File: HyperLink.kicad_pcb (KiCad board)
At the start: 2 copper layers, 35 x 24 mm, 45 parts, among them J1 USB_C_Receptacle_USB2.0, J2 Conn_02x05_Odd_Even, J3 Conn_02x05_Odd_Even, SW1 SW_Push, U1 ESP32-C3, U2 PESD2USB5UXT, U3 MIC5504-3.3YM5, Y1 ABM11W-40.0000MHZ-8-B1U-T3

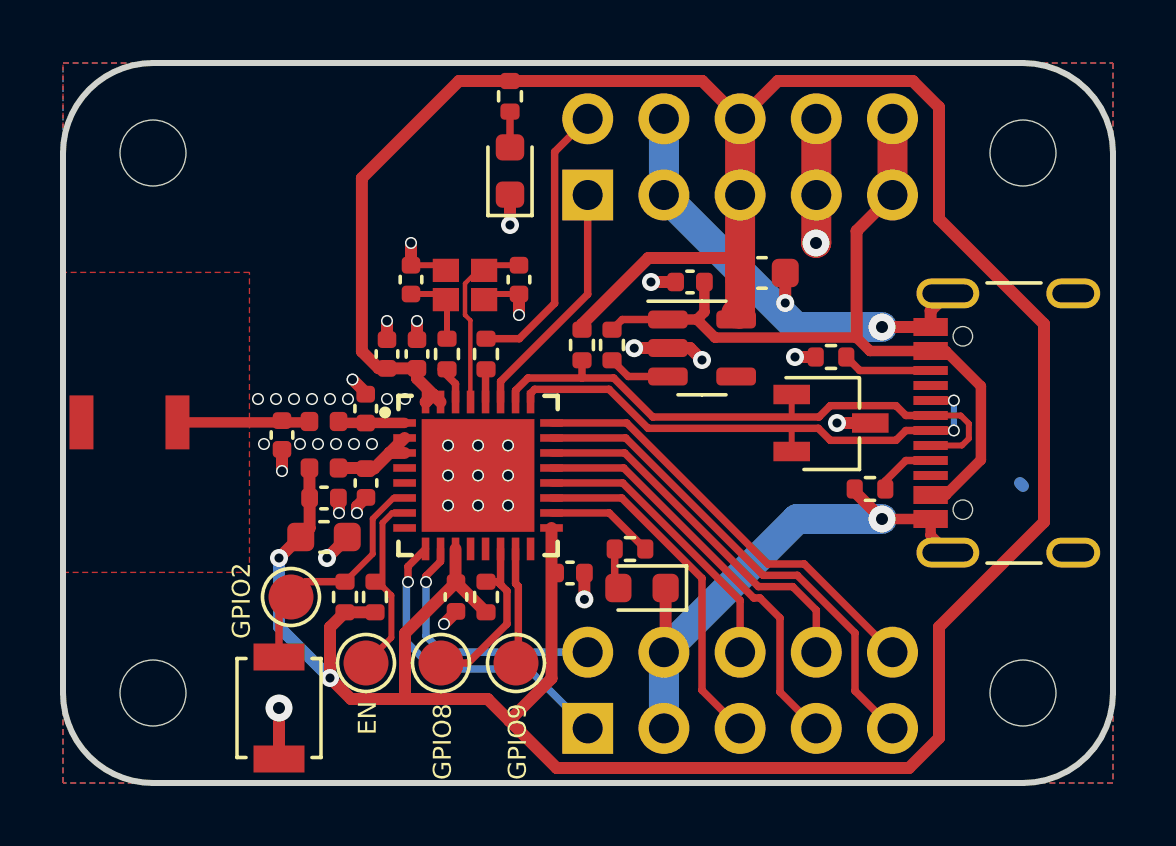
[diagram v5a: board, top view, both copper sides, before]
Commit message: Add via stitching
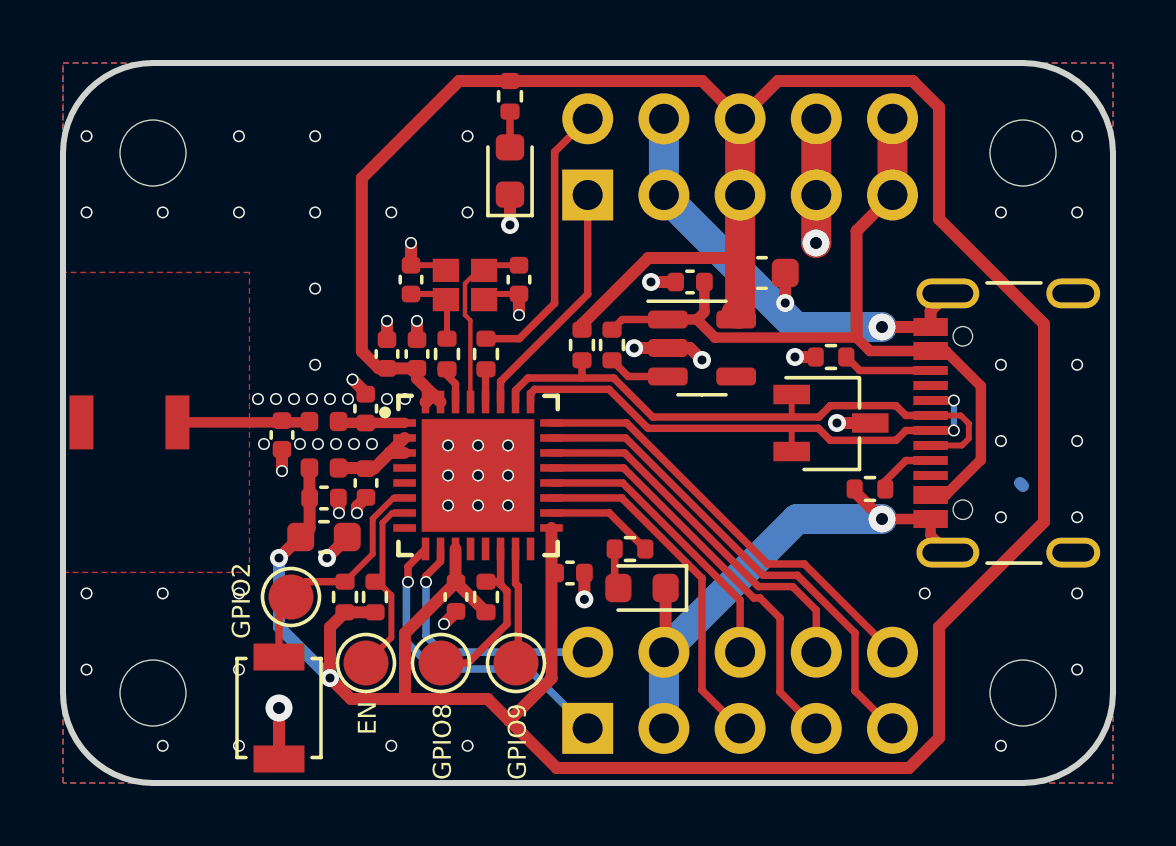
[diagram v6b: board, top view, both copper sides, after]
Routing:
- net GND: vias 45 -> 79
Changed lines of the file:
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@@
   (segment (start 132.1 88.3) (end 132.1 88.28) (width 0.4) (layer "F.Cu") (net 5))
   (segment (start 144.11 75.99) (end 144.1 76) (width 1) (layer "F.Cu") (net 5))
+  (via (at 127.405 74.979999) (size 0.4) (drill 0.3) (layers "F.Cu" "B.Cu") (free) (net 5))
+  (via (at 132.485 72.439999) (size 0.4) (drill 0.3) (layers "F.Cu" "B.Cu") (free) (net 5))
+  (via (at 122.325 92.759999) (size 0.4) (drill 0.3) (layers "F.Cu" "B.Cu") (free) (net 5))
   (via (at 130.4 81.2) (size 0.4) (drill 0.3) (layers "F.Cu" "B.Cu") (free) (net 5))
   (via (at 128.65 80.55) (size 0.4) (drill 0.3) (layers "F.Cu" "B.Cu") (free) (net 5))
   (via (at 126.9 82.7) (size 0.4) (drill 0.3) (layers "F.Cu" "B.Cu") (free) (net 5))
+  (via (at 119.785 72.439999) (size 0.4) (drill 0.3) (layers "F.Cu" "B.Cu") (free) (net 5))
   (via (at 138.6 77.3) (size 0.6) (drill 0.3) (layers "F.Cu" "B.Cu") (net 5))
   (via (at 129.8 81.2) (size 0.4) (drill 0.3) (layers "F.Cu" "B.Cu") (free) (net 5))
+  (via (at 152.805 87.679999) (size 0.4) (drill 0.3) (layers "F.Cu" "B.Cu") (free) (net 5))
+  (via (at 147.725 87.679999) (size 0.4) (drill 0.3) (layers "F.Cu" "B.Cu") (free) (net 5))
   (via (at 133.9 75.4) (size 0.6) (drill 0.3) (layers "F.Cu" "B.Cu") (net 5))
   (via (at 128.1 82.7) (size 0.4) (drill 0.3) (layers "F.Cu" "B.Cu") (free) (net 5))
+  (via (at 124.865 92.759999) (size 0.4) (drill 0.3) (layers "F.Cu" "B.Cu") (free) (net 5))
+  (via (at 132.485 74.979999) (size 0.4) (drill 0.3) (layers "F.Cu" "B.Cu") (free) (net 5))
   (via (at 146.3 78.8) (size 0.9) (drill 0.4) (layers "F.Cu" "B.Cu") (free) (net 5))
   (via (at 133.834851 84.7487) (size 0.4) (drill 0.3) (layers "F.Cu" "B.Cu") (net 5))
@@
   (via (at 131.834851 84.7487) (size 0.4) (drill 0.3) (layers "F.Cu" "B.Cu") (net 5))
   (via (at 127.5 82.7) (size 0.4) (drill 0.3) (layers "F.Cu" "B.Cu") (free) (net 5))
+  (via (at 152.805 74.979999) (size 0.4) (drill 0.3) (layers "F.Cu" "B.Cu") (free) (net 5))
+  (via (at 127.405 80.059999) (size 0.4) (drill 0.3) (layers "F.Cu" "B.Cu") (free) (net 5))
   (via (at 136.38 87.88) (size 0.6) (drill 0.3) (layers "F.Cu" "B.Cu") (free) (net 5))
   (via (at 143.075 78) (size 0.6) (drill 0.3) (layers "F.Cu" "B.Cu") (net 5))
   (via (at 138.040639 79.505918) (size 0.6) (drill 0.3) (layers "F.Cu" "B.Cu") (net 5))
   (via (at 131.834851 83.7487) (size 0.4) (drill 0.3) (layers "F.Cu" "B.Cu") (net 5))
+  (via (at 124.865 72.439999) (size 0.4) (drill 0.3) (layers "F.Cu" "B.Cu") (free) (net 5))
   (via (at 144.8 82) (size 0.6) (drill 0.3) (layers "F.Cu" "B.Cu") (net 5))
   (via (at 132.834851 82.7487) (size 0.4) (drill 0.3) (layers "F.Cu" "B.Cu") (net 5))
+  (via (at 124.865 74.979999) (size 0.4) (drill 0.3) (layers "F.Cu" "B.Cu") (free) (net 5))
   (via (at 130.6 76) (size 0.4) (drill 0.3) (layers "F.Cu" "B.Cu") (free) (net 5))
+  (via (at 150.265 74.979999) (size 0.4) (drill 0.3) (layers "F.Cu" "B.Cu") (free) (net 5))
+  (via (at 124.865 87.679999) (size 0.4) (drill 0.3) (layers "F.Cu" "B.Cu") (free) (net 5))
   (via (at 126.2 91.5) (size 0.9) (drill 0.4) (layers "F.Cu" "B.Cu") (net 5))
+  (via (at 150.265 92.759999) (size 0.4) (drill 0.3) (layers "F.Cu" "B.Cu") (free) (net 5))
   (via (at 128.799503 85) (size 0.4) (drill 0.3) (layers "F.Cu" "B.Cu") (free) (net 5))
+  (via (at 127.405 72.439999) (size 0.4) (drill 0.3) (layers "F.Cu" "B.Cu") (free) (net 5))
   (via (at 143.4 79.8) (size 0.6) (drill 0.3) (layers "F.Cu" "B.Cu") (net 5))
+  (via (at 119.785 87.679999) (size 0.4) (drill 0.3) (layers "F.Cu" "B.Cu") (free) (net 5))
   (via (at 133.834851 83.7487) (size 0.4) (drill 0.3) (layers "F.Cu" "B.Cu") (net 5))
+  (via (at 152.805 90.219999) (size 0.4) (drill 0.3) (layers "F.Cu" "B.Cu") (free) (net 5))
+  (via (at 152.805 85.139999) (size 0.4) (drill 0.3) (layers "F.Cu" "B.Cu") (free) (net 5))
   (via (at 131.834851 82.7487) (size 0.4) (drill 0.3) (layers "F.Cu" "B.Cu") (net 5))
   (via (at 127.3 81.2) (size 0.4) (drill 0.3) (layers "F.Cu" "B.Cu") (free) (net 5))
+  (via (at 122.325 87.679999) (size 0.4) (drill 0.3) (layers "F.Cu" "B.Cu") (free) (net 5))
+  (via (at 119.785 90.219999) (size 0.4) (drill 0.3) (layers "F.Cu" "B.Cu") (free) (net 5))
   (via (at 128.7 82.7) (size 0.4) (drill 0.3) (layers "F.Cu" "B.Cu") (free) (net 5))
+  (via (at 152.805 80.059999) (size 0.4) (drill 0.3) (layers "F.Cu" "B.Cu") (free) (net 5))
   (via (at 129.8 78.6) (size 0.4) (drill 0.3) (layers "F.Cu" "B.Cu") (free) (net 5))
   (via (at 132.834851 84.7487) (size 0.4) (drill 0.3) (layers "F.Cu" "B.Cu") (net 5))
+  (via (at 122.325 74.979999) (size 0.4) (drill 0.3) (layers "F.Cu" "B.Cu") (free) (net 5))
   (via (at 126.3 83.6) (size 0.4) (drill 0.3) (layers "F.Cu" "B.Cu") (free) (net 5))
+  (via (at 152.805 82.599999) (size 0.4) (drill 0.3) (layers "F.Cu" "B.Cu") (free) (net 5))
+  (via (at 129.945 92.759999) (size 0.4) (drill 0.3) (layers "F.Cu" "B.Cu") (free) (net 5))
   (via (at 130.8 78.6) (size 0.4) (drill 0.3) (layers "F.Cu" "B.Cu") (free) (net 5))
   (via (at 146.3 85.2) (size 0.9) (drill 0.4) (layers "F.Cu" "B.Cu") (free) (net 5))
   (via (at 125.7 82.7) (size 0.4) (drill 0.3) (layers "F.Cu" "B.Cu") (free) (net 5))
+  (via (at 150.265 85.139999) (size 0.4) (drill 0.3) (layers "F.Cu" "B.Cu") (free) (net 5))
   (via (at 140.3 79.9) (size 0.6) (drill 0.3) (layers "F.Cu" "B.Cu") (net 5))
+  (via (at 132.485 92.759999) (size 0.4) (drill 0.3) (layers "F.Cu" "B.Cu") (free) (net 5))
   (via (at 128.2 85) (size 0.4) (drill 0.3) (layers "F.Cu" "B.Cu") (free) (net 5))
+  (via (at 129.945 74.979999) (size 0.4) (drill 0.3) (layers "F.Cu" "B.Cu") (free) (net 5))
   (via (at 129.3 82.7) (size 0.4) (drill 0.3) (layers "F.Cu" "B.Cu") (free) (net 5))
+  (via (at 119.785 74.979999) (size 0.4) (drill 0.3) (layers "F.Cu" "B.Cu") (free) (net 5))
   (via (at 126.099503 81.2) (size 0.4) (drill 0.3) (layers "F.Cu" "B.Cu") (free) (net 5))
   (via (at 144.1 76) (size 0.9) (drill 0.4) (layers "F.Cu" "B.Cu") (free) (net 5))
@@
   (via (at 125.5 81.2) (size 0.4) (drill 0.3) (layers "F.Cu" "B.Cu") (free) (net 5))
   (via (at 131.7 88.7) (size 0.4) (drill 0.3) (layers "F.Cu" "B.Cu") (free) (net 5))
+  (via (at 152.805 72.439999) (size 0.4) (drill 0.3) (layers "F.Cu" "B.Cu") (free) (net 5))
   (via (at 127.9 81.2) (size 0.4) (drill 0.3) (layers "F.Cu" "B.Cu") (free) (net 5))
+  (via (at 124.865 90.219999) (size 0.4) (drill 0.3) (layers "F.Cu" "B.Cu") (free) (net 5))
   (via (at 128.5 81.2) (size 0.4) (drill 0.3) (layers "F.Cu" "B.Cu") (free) (net 5))
   (via (at 127.8 86.5) (size 0.6) (drill 0.3) (layers "F.Cu" "B.Cu") (free) (net 5))
+  (via (at 150.265 80.059999) (size 0.4) (drill 0.3) (layers "F.Cu" "B.Cu") (free) (net 5))
+  (via (at 150.265 82.599999) (size 0.4) (drill 0.3) (layers "F.Cu" "B.Cu") (free) (net 5))
+  (via (at 127.405 77.519999) (size 0.4) (drill 0.3) (layers "F.Cu" "B.Cu") (free) (net 5))
   (segment (start 143.43 78.8) (end 146.3 78.8) (width 1) (layer "B.Cu") (net 5))
   (segment (start 139.03 92.18) (end 139.03 89.64) (width 1) (layer "B.Cu") (net 5))
@@
     )
   )
+  (group "ViaStitching GND" (id 121eea07-2583-43eb-af17-1480b4d71986)
+    (members
+      00bb237d-837b-4d5a-bcef-fa8cfbdb1b4f
+      06f155e1-c9e6-4bee-978f-681a4968c2e1
+      08c9f7d6-f1ce-4e30-9afb-da5f94dd47ce
+      0e67f340-c2e4-46b6-9b0b-a6d67aab93a5
+      220ef5ba-ac45-4e73-99d3-577b26c0473a
+      23bdd84b-9662-4baf-8c54-9a2bf71ae2ce
+      2ef98852-6df9-4ee1-8d35-f6a4a30a555b
+      31b7294f-a97f-4f42-8ae6-3d87eb07fe97
+      4b072cb5-440d-463b-9ff8-211d0f28688c
+      4ddd4fa3-a042-4c53-b063-b147359e3cbb
+      557f1756-ca36-4d67-9c0f-42117ab397c9
+      64ec0c78-07fc-4cba-ac41-35cad36918ec
+      66550240-bda5-475f-a09d-6517f8722017
+      66df1f4a-5b2c-46ef-a507-0858b39ec60e
+      6f2b45b0-d9ce-4335-b6ee-ab0727387dc2
+      71b87463-798a-4e1b-b2ef-059b92664430
+      7909f0ca-0463-4a9e-aaaf-f561e94ccda1
+      8144d179-87ba-4135-95e5-eb17538a4128
+      82302608-db9a-48ed-8ab8-dbf81359da0a
+      8a3a5948-1c3f-481c-a79a-a6d3abd361df
+      8b6986c9-79fc-451d-ae15-52141ac0a98d
+      a06ebc2b-7ec2-4ced-b829-606dcd57b138
+      ae848523-224c-499e-a046-5a96c8e42e0b
+      af48a8c5-db91-40cd-8115-ac9e1430a562
+      afd6c00a-8791-4bc7-8efe-20083c53a3f2
+      b47e8231-2c8a-4498-8e5b-560701a50b27
+      bd334d69-a12f-40be-8870-ccd59f2fb445
+      c4102dce-062b-4627-9724-f3663cb34ef7
+      c4b117e6-d985-4fe9-8e23-5f7d37895993
+      dfaad4b6-1565-4988-ad73-fac53e226262
+      e5cb9263-b40f-4e25-9610-8460d1c975e1
+      ecf5bfc4-d903-424e-9227-a9dc3abac6d9
+      ef14ce98-ae78-46c5-a63f-b8e6ad8087e2
+      fdd36023-d493-4760-ad84-780c0c0c6f70
+    )
+  )

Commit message: Flip D+ and D- at connector
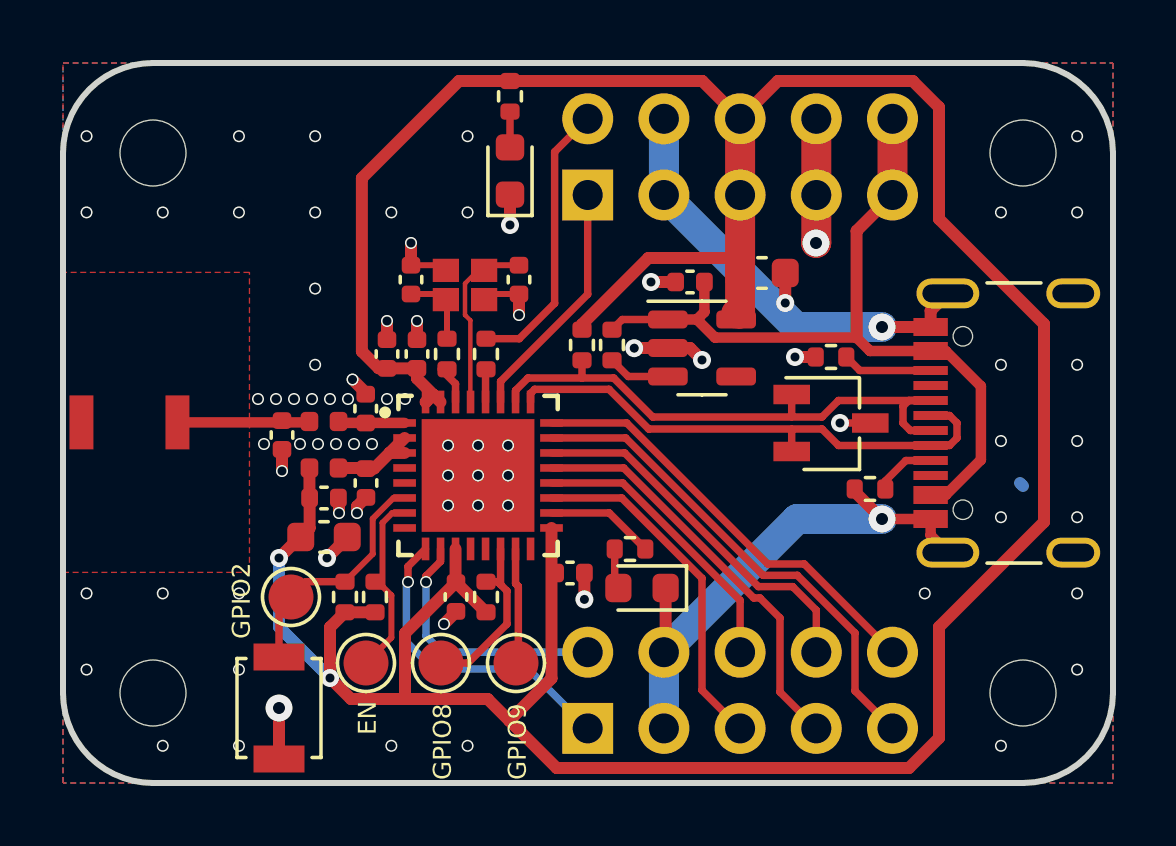
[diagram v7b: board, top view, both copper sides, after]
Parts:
- removed R9: 1k5, Resistor_SMD:R_0402_1005Metric
- added R1: 1k5, Resistor_SMD:R_0402_1005Metric, F.Cu at (136.3, 79.4)
- C5, C6: value 10pF -> 10p
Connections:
- J1 pad A6: /USB_D- -> /USB_D+
- J1 pad A7: /USB_D+ -> /USB_D-
- J1 pad B6: /USB_D- -> /USB_D+
- J1 pad B7: /USB_D+ -> /USB_D-
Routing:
- net /USB_D+: track 19.9 -> 19.1 mm
- net /USB_D-: track 17.8 -> 17.7 mm, vias 2 -> 0
